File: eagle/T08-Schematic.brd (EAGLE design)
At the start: 65.8 x 25.4 mm, 69 parts, among them IC1 BQ24022, J1 USB-MICROB, J3 JST-PH-2-SMT-RA, U1 LP5907, U2 M25P10-AVMN6TP_TR, U3 LSM9DS0, U5 LTC1998, U6 ATMEGA32U4-AU, X1 8MHz

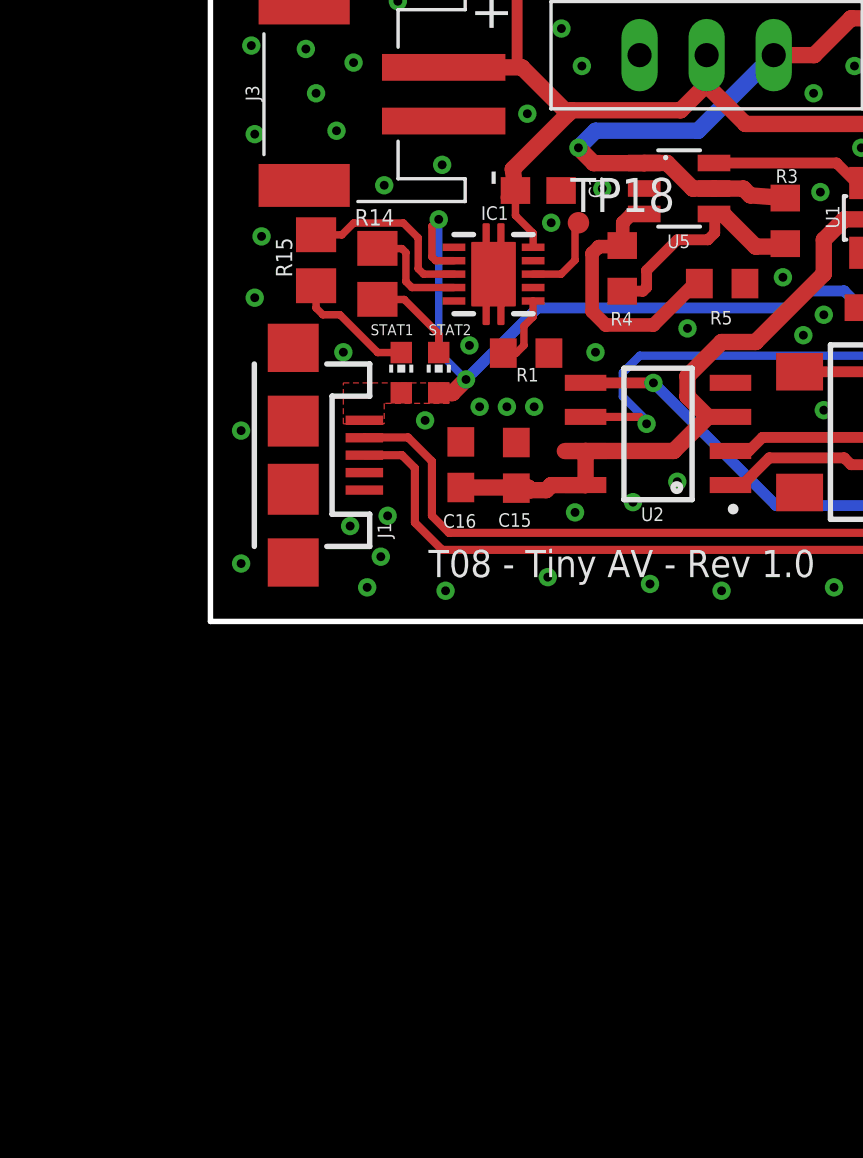
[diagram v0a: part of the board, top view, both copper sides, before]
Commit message: Added device for charging chip, and created footprint and device for sensor.
Also began reworking schematic.
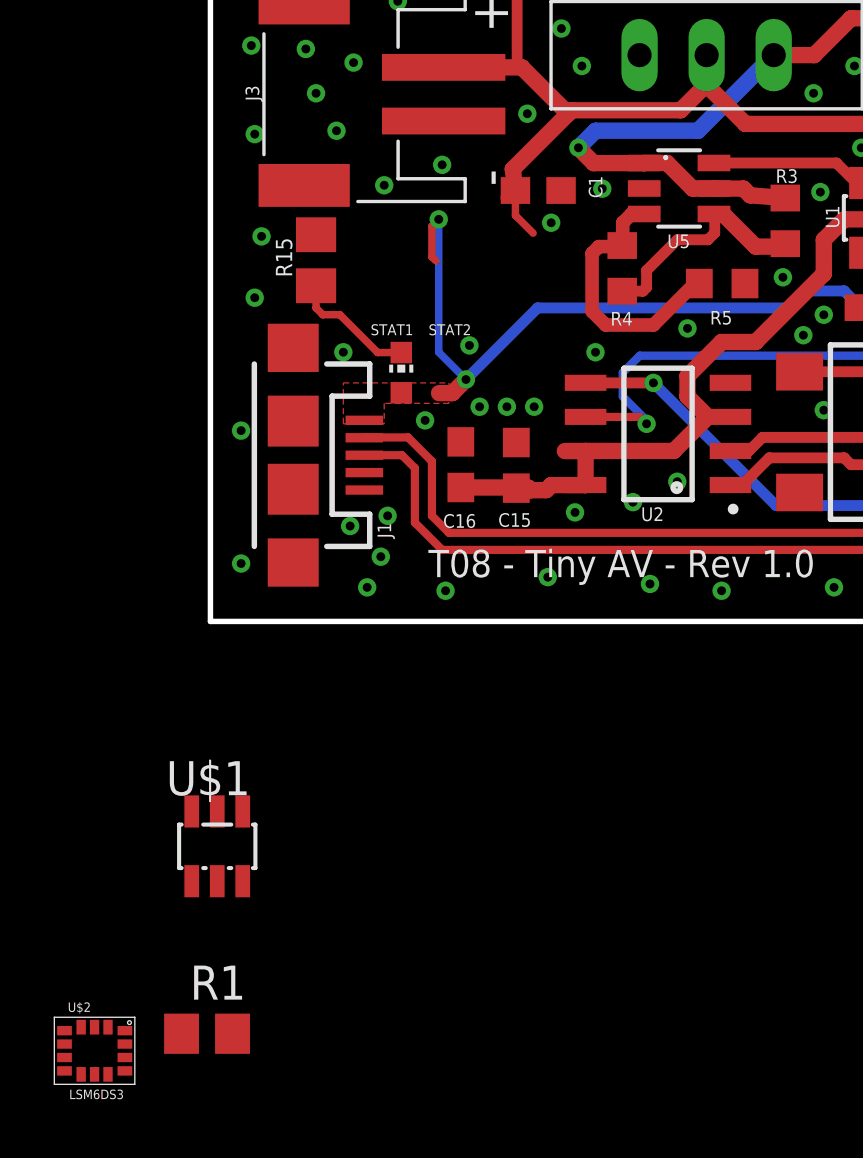
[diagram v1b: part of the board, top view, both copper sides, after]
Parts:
- removed IC1: BQ24022, tinyav-lib:DRC-S-PVSON-N10
- removed LED3: (no value), adafruit:CHIP-LED0603
- removed R14: 330, rcl:R0805
- removed TP18: TPTP08R, testpad:TP08R
- added U$1: BQ21040, tinyav-lib:SOT23-6L
- added U$2: LSM6DS3, tinyav-lib:LGA-14L
- R1: value 4k -> 5.36k; device rcl:R0603 -> rcl:R0805
- R15, R16, R6, R7, R8: value 330 -> 3.3k
- moved R1 28.0 mm to (-0.13, -15.4), turned to 0 degrees
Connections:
- removed net N$50: IC1.3, R15.2
- removed net N$51: IC1.4, R14.2
- removed net N$68: IC1.8, TP18.TP
- net GND: now also U$1.5; no longer IC1.5, IC1.7, IC1.9
- net N$13: now also U$1.2; no longer IC1.10
- net N$4: now also R15.2, U$1.3; no longer IC1.6, R1.2
- net N$49: now also R1.2, U$1.4; no longer LED3.C, R14.1
- net VBUS1: now also U$1.6; no longer IC1.2, LED3.A
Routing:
- net N$50: track 6.79 -> 0.00 mm
- net N$51: track 4.10 -> 0.00 mm
- net N$49: track 3.51 -> 0.00 mm
- net N$68: track 3.23 -> 0.00 mm
- net N$4: track 2.69 -> 0.00 mm
- net VBUS1: track 62.8 -> 62.1 mm
- net N$13: track 35.7 -> 35.1 mm
